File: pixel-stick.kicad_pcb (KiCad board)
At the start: 2 copper layers, 44 x 20.5 mm, 20 parts, among them J1 WS281*, J2 ISP, Q1 BSS138, SW1 RESET, SW2 PROG, U1 LM3670MF, U2 RT9361A, U4 ESP-M2

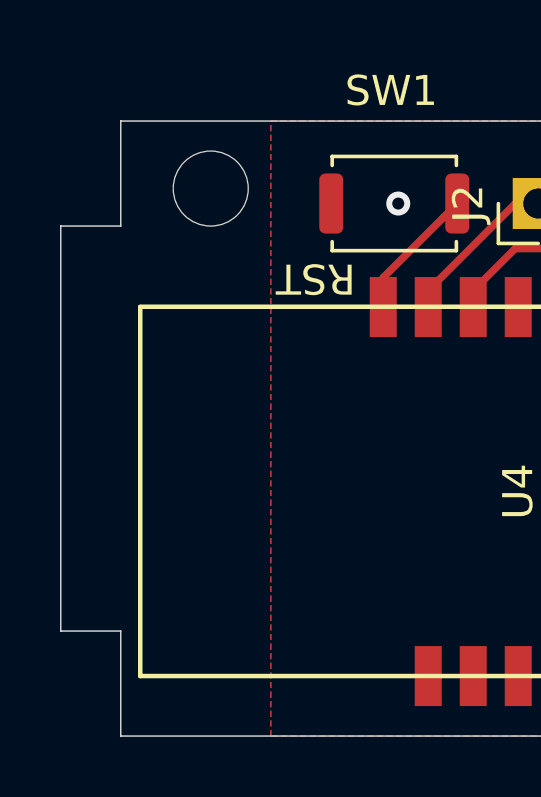
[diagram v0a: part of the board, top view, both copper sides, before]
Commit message: trim excess pcb
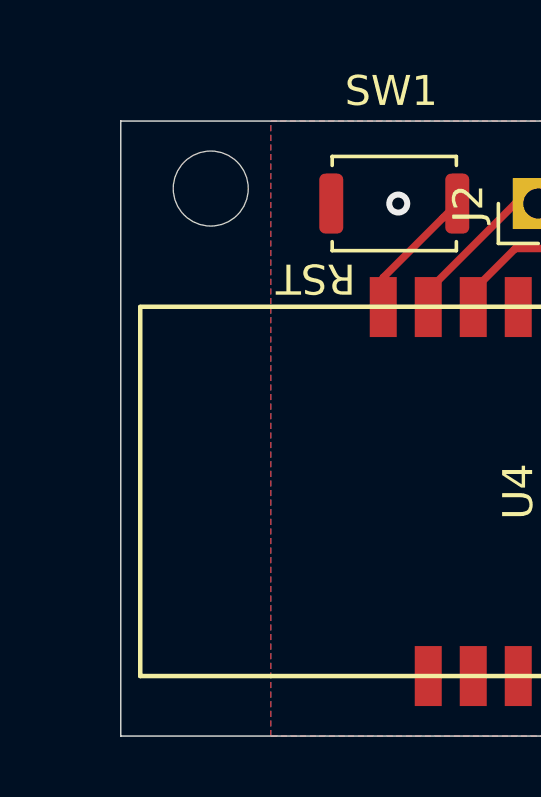
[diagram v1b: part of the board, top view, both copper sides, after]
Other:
- board size 44 x 20.5 mm -> 42 x 20.5 mm
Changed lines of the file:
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@@
   (general
     (thickness 1.6)
-    (drawings 18)
+    (drawings 14)
     (tracks 103)
     (zones 0)
@@
     )
   )
+  (gr_line (start 72 28.5) (end 72 49) (layer Edge.Cuts) (width 0.05))
   (gr_text RST (at 78.5 33.75 180) (layer F.SilkS)
     (effects (font (size 1 1) (thickness 0.15)))
@@
   (gr_line (start 110.5 30.2) (end 114 30.2) (layer Edge.Cuts) (width 0.05))
   (gr_line (start 110.5 28.5) (end 110.5 30.2) (layer Edge.Cuts) (width 0.05))
-  (gr_line (start 72 45.5) (end 70 45.5) (layer Edge.Cuts) (width 0.05))
-  (gr_line (start 72 49) (end 72 45.5) (layer Edge.Cuts) (width 0.05))
-  (gr_line (start 72 32) (end 70 32) (layer Edge.Cuts) (width 0.05))
-  (gr_line (start 72 28.5) (end 72 32) (layer Edge.Cuts) (width 0.05))
-  (gr_line (start 70 32) (end 70 45.5) (layer Edge.Cuts) (width 0.05))
   (gr_line (start 110.5 28.5) (end 72 28.5) (layer Edge.Cuts) (width 0.05))
   (gr_line (start 114 47.3) (end 114 30.2) (layer Edge.Cuts) (width 0.05))

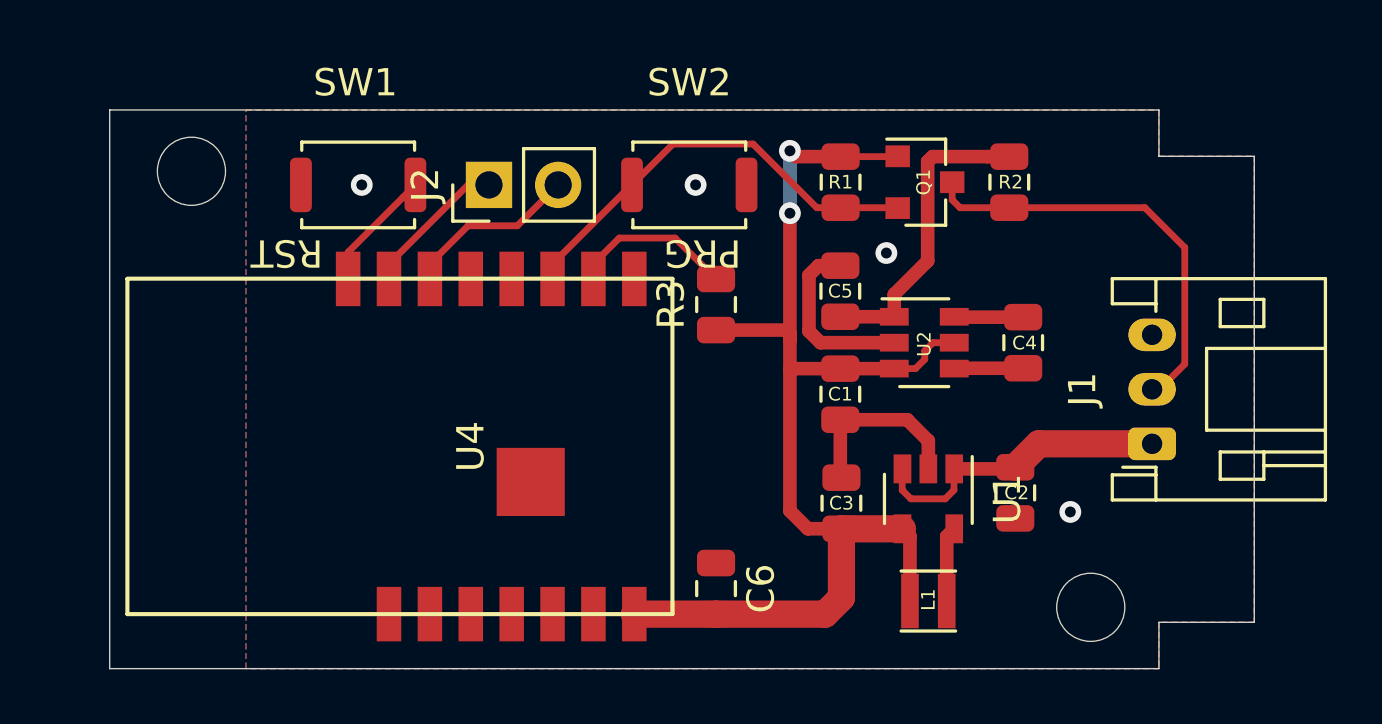
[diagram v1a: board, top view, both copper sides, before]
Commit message: make design work for ESP-01 or ESP-M2
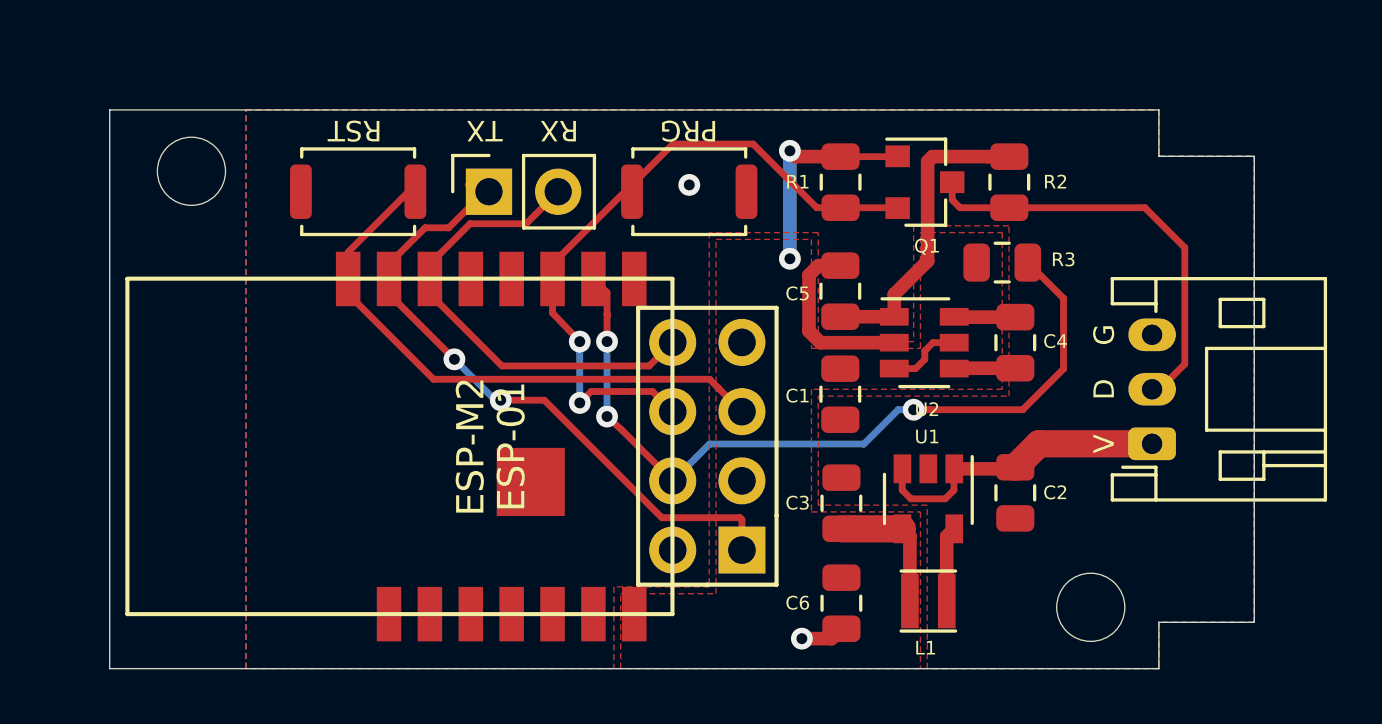
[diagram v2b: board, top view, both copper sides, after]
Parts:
- added ESP-01: ESP-01v090, ESP8266:ESP-01, F.Cu at (95.2, 44.6)
- J2: footprint Connector_PinHeader_2.54mm:PinHeader_1x02_P2.54mm_Vertical -> Connector_PinSocket_2.54mm:PinSocket_1x02_P2.54mm_Vertical
- moved R3 10.6 mm to (104.8, 34.1), turned to 0 degrees
- moved C6 4.63 mm to (98.8, 46.6), turned to 90 degrees
- moved C4 0.29 mm to (105.2, 37.0)
- moved J2 0.25 mm to (85.9, 31.5)
- moved SW1 0.25 mm to (81.1, 31.5)
- moved SW2 0.25 mm to (93.3, 31.5)
- renumbered U4 to ESP-M2
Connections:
- net Net-(R3-Pad2) renamed /GPIO2
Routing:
- net +3V3: track 44.4 -> 15.9 mm
- net /GPIO2: track 6.07 -> 30.5 mm, vias 0 -> 3
- net /TXD: track 5.42 -> 24.2 mm, vias 0 -> 2
- net /RST: track 4.47 -> 21.3 mm
- net /RXD: track 6.46 -> 17.3 mm
- net /GPIO0: track 16.0 -> 24.9 mm, vias 0 -> 2
- net GND: track 13.4 -> 8.26 mm, vias 4 -> 2
- added copper zone on F.Cu, net +3V3
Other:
- board text added: "D"
- board text added: "G"
- board text added: "RX"
- board text added: "TX"
- board text added: "V"

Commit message: remove resistor from GPIO2 pull-up
may have been a bad idea ... will need to check that things still work. Its possible the ESP-01 and ESP-M2 have internal pull ups alredy enabled and I can remove the external 3V3 entirely.
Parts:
- removed R3: 10k, Resistor_SMD:R_0805_2012Metric
- J2: footprint Connector_PinSocket_2.54mm:PinSocket_1x02_P2.54mm_Vertical -> Connector_PinHeader_2.54mm:PinHeader_1x02_P2.54mm_Vertical
- renumbered ESP-01 to U3, ESP-M2 to U4
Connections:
- U3 pad 4: /GPIO2 -> +3V3
- U4 pad 9: /GPIO2 -> +3V3
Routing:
- net /GPIO2: track 30.5 -> 0.00 mm, vias 3 -> 0
- net +3V3: track 15.9 -> 25.9 mm, vias 2 -> 4
- net /DATA: track 15.8 -> 11.9 mm
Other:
- board text added: "Board Version: 20191218a"
- board text removed: "Board Version: 20191217a"

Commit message: Add R3 back to GPIO2
Also re-laid out the microcontrollers in schematic to make it clearer how the common interface is achieved.
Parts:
- added R3: 10k, Resistor_SMD:R_0805_2012Metric, F.Cu at (104.3, 34.0)
- J2: value ISP -> ICSP
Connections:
- U3 pad 4: +3V3 -> /GPIO2
- U4 pad 9: +3V3 -> /GPIO2
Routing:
- net /GPIO2: track 0.00 -> 30.8 mm, vias 0 -> 3
- net +3V3: track 25.9 -> 15.9 mm, vias 4 -> 2
- net /DATA: track 11.9 -> 14.2 mm
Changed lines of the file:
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@@
     (thickness 1.6)
     (drawings 19)
-    (tracks 123)
+    (tracks 138)
     (zones 0)
-    (modules 20)
-    (nets 22)
+    (modules 21)
+    (nets 23)
   )
   (page A4)
@@
   (net 20 "Net-(U4-Pad2)")
   (net 21 "Net-(U3-Pad3)")
+  (net 22 /GPIO2)
   (net_class Default "This is the default net class."
     (clearance 0.2)
@@
     (add_net /DATA)
     (add_net /GPIO0)
+    (add_net /GPIO2)
     (add_net /RST)
     (add_net /RXD)
@@
     (add_net VIN)
   )
+  (module Resistor_SMD:R_0805_2012Metric (layer F.Cu)
+    (at 104.3125 34)
+    (descr "Resistor SMD 0805 (2012 Metric), square (rectangular) end terminal, IPC_7351 nominal, (Body size source: https://docs.google.com/spreadsheets/d/1BsfQQcO9C6DZCsRaXUlFlo91Tg2WpOkGARC1WS5S8t0/edit?usp=sharing), generated with kicad-footprint-generator")
+    (tags resistor)
+    (attr smd)
+    (fp_text reference R3 (at 2.3975 0) (layer F.SilkS)
+      (effects (font (size 0.5 0.5) (thickness 0.125)))
+    )
+    (fp_text value 10k (at 0 1.65) (layer F.Fab)
+      (effects (font (size 1 1) (thickness 0.15)))
+    )
+    (fp_text user %R (at 0 0) (layer F.Fab)
+      (effects (font (size 0.5 0.5) (thickness 0.08)))
+    )
+    (fp_line (start 1.68 0.95) (end -1.68 0.95) (layer F.CrtYd) (width 0.05))
+    (fp_line (start 1.68 -0.95) (end 1.68 0.95) (layer F.CrtYd) (width 0.05))
+    (fp_line (start -1.68 -0.95) (end 1.68 -0.95) (layer F.CrtYd) (width 0.05))
+    (fp_line (start -1.68 0.95) (end -1.68 -0.95) (layer F.CrtYd) (width 0.05))
+    (fp_line (start -0.258578 0.71) (end 0.258578 0.71) (layer F.SilkS) (width 0.12))
+    (fp_line (start -0.258578 -0.71) (end 0.258578 -0.71) (layer F.SilkS) (width 0.12))
+    (fp_line (start 1 0.6) (end -1 0.6) (layer F.Fab) (width 0.1))
+    (fp_line (start 1 -0.6) (end 1 0.6) (layer F.Fab) (width 0.1))
+    (fp_line (start -1 -0.6) (end 1 -0.6) (layer F.Fab) (width 0.1))
+    (fp_line (start -1 0.6) (end -1 -0.6) (layer F.Fab) (width 0.1))
+    (pad 2 smd roundrect (at 0.9375 0) (size 0.975 1.4) (layers F.Cu F.Paste F.Mask) (roundrect_rratio 0.25)
+      (net 22 /GPIO2))
+    (pad 1 smd roundrect (at -0.9375 0) (size 0.975 1.4) (layers F.Cu F.Paste F.Mask) (roundrect_rratio 0.25)
+      (net 2 +3V3))
+    (model ${KISYS3DMOD}/Resistor_SMD.3dshapes/R_0805_2012Metric.wrl
+      (at (xyz 0 0 0))
+      (scale (xyz 1 1 1))
+      (rotate (xyz 0 0 0))
+    )
+  )
   (module Connector_PinHeader_2.54mm:PinHeader_1x02_P2.54mm_Vertical locked (layer F.Cu)
     (at 85.917499 31.5 90)
@@
       (effects (font (size 1 1) (thickness 0.15)))
     )
-    (fp_text value ISP (at 0 4.87 90) (layer F.Fab)
+    (fp_text value ICSP (at 0 4.87 90) (layer F.Fab)
       (effects (font (size 1 1) (thickness 0.15)))
     )
@@
       (net 13 /RST))
     (pad 4 thru_hole oval (at 2.54 2.54 180) (size 1.7272 1.7272) (drill 1.016) (layers *.Cu *.Mask F.SilkS)
-      (net 2 +3V3))
+      (net 22 /GPIO2))
     (pad 3 thru_hole oval (at 0 2.54 180) (size 1.7272 1.7272) (drill 1.016) (layers *.Cu *.Mask F.SilkS)
       (net 21 "Net-(U3-Pad3)"))
@@
       (net 5 /GPIO0))
     (pad 9 smd rect (at 6.15 4.5 180) (size 0.9 2) (layers F.Cu F.Paste F.Mask)
-      (net 2 +3V3))
+      (net 22 /GPIO2))
     (pad 8 smd rect (at 6.15 6 180) (size 0.9 2) (layers F.Cu F.Paste F.Mask)
       (net 1 GND))
@@
   (segment (start 96.95998 30) (end 96.95998 33.95998) (width 0.5) (layer B.Cu) (net 2))
   (segment (start 96.95998 34.09002) (end 96.95998 33.95998) (width 0.5) (layer F.Cu) (net 2))
-  (segment (start 90.25 37) (end 90.25 36.9) (width 0.25) (layer B.Cu) (net 2))
-  (segment (start 90.25 36.9) (end 90.25 39.75) (width 0.25) (layer B.Cu) (net 2))
-  (segment (start 90.25 36) (end 90.25 35.2) (width 0.25) (layer F.Cu) (net 2))
-  (segment (start 90.275001 36.025001) (end 90.25 36) (width 0.25) (layer F.Cu) (net 2))
-  (segment (start 90.25 37) (end 90.25 36) (width 0.25) (layer F.Cu) (net 2))
-  (segment (start 90.25 35.2) (end 89.75 34.7) (width 0.25) (layer F.Cu) (net 2))
-  (via (at 90.25 39.75) (size 0.8) (drill 0.4) (layers F.Cu B.Cu) (net 2))
-  (segment (start 89.75 34.7) (end 89.75 35.25) (width 0.25) (layer F.Cu) (net 2))
-  (via (at 90.25 37) (size 0.8) (drill 0.4) (layers F.Cu B.Cu) (net 2))
-  (segment (start 90.8 40.25) (end 92.66 42.11) (width 0.25) (layer F.Cu) (net 2))
-  (segment (start 90.25 39.75) (end 90.8 40.25) (width 0.25) (layer F.Cu) (net 2))
-  (segment (start 89.75 34.7) (end 89.75 34.15) (width 0.25) (layer F.Cu) (net 2))
+  (segment (start 90.25 37) (end 90.25 36.9) (width 0.25) (layer B.Cu) (net 22))
+  (segment (start 90.25 36.9) (end 90.25 39.75) (width 0.25) (layer B.Cu) (net 22))
+  (segment (start 90.25 36) (end 90.25 35.2) (width 0.25) (layer F.Cu) (net 22))
+  (segment (start 90.275001 36.025001) (end 90.25 36) (width 0.25) (layer F.Cu) (net 22))
+  (segment (start 90.25 37) (end 90.25 36) (width 0.25) (layer F.Cu) (net 22))
+  (segment (start 90.25 35.2) (end 89.75 34.7) (width 0.25) (layer F.Cu) (net 22))
+  (via (at 90.25 39.75) (size 0.8) (drill 0.4) (layers F.Cu B.Cu) (net 22))
+  (segment (start 89.75 34.7) (end 89.75 35.25) (width 0.25) (layer F.Cu) (net 22))
+  (via (at 90.25 37) (size 0.8) (drill 0.4) (layers F.Cu B.Cu) (net 22))
+  (segment (start 90.8 40.25) (end 92.66 42.11) (width 0.25) (layer F.Cu) (net 22))
+  (segment (start 90.25 39.75) (end 90.8 40.25) (width 0.25) (layer F.Cu) (net 22))
+  (segment (start 89.75 34.7) (end 89.75 34.15) (width 0.25) (layer F.Cu) (net 22))
   (segment (start 100.785 36.085) (end 100.79 36.09) (width 0.5) (layer F.Cu) (net 3))
   (segment (start 100.7875 36.0875) (end 100.79 36.09) (width 0.5) (layer F.Cu) (net 3))
@@
   (segment (start 105.01 32.0875) (end 103.2025 32.0875) (width 0.25) (layer F.Cu) (net 4))
   (segment (start 109.975 38.75) (end 110.25 38.75) (width 0.25) (layer F.Cu) (net 4))
-  (segment (start 105.01 33.785) (end 109.975 38.75) (width 0.25) (layer F.Cu) (net 4))
-  (segment (start 105.01 32.0875) (end 105.01 33.785) (width 0.25) (layer F.Cu) (net 4))
+  (segment (start 107.131247 33.408747) (end 107.131247 38.618753) (width 0.25) (layer F.Cu) (net 4))
+  (segment (start 105.01 32.0875) (end 105.81 32.0875) (width 0.25) (layer F.Cu) (net 4))
+  (segment (start 105.81 32.0875) (end 107.131247 33.408747) (width 0.25) (layer F.Cu) (net 4))
+  (segment (start 107.262494 38.75) (end 110.25 38.75) (width 0.25) (layer F.Cu) (net 4))
+  (segment (start 107.131247 38.618753) (end 107.262494 38.75) (width 0.25) (layer F.Cu) (net 4))
   (segment (start 88.25 34.15) (end 91.15 31.25) (width 0.25) (layer F.Cu) (net 5))
   (segment (start 91.15 31.25) (end 91.167499 31.25) (width 0.25) (layer F.Cu) (net 5))
@@
   (segment (start 80.75 35.25) (end 83.881399 38.381399) (width 0.25) (layer F.Cu) (net 13))
   (segment (start 80.75 34.7) (end 80.75 35.25) (width 0.25) (layer F.Cu) (net 13))
+  (segment (start 106.681237 34.556237) (end 106.681237 38.030613) (width 0.25) (layer F.Cu) (net 22))
+  (segment (start 106.125 34) (end 106.681237 34.556237) (width 0.25) (layer F.Cu) (net 22))
+  (segment (start 105.480925 39.230925) (end 100.519075 39.230925) (width 0.25) (layer F.Cu) (net 22))
+  (segment (start 106.681237 38.030613) (end 105.480925 39.230925) (width 0.25) (layer F.Cu) (net 22))
+  (segment (start 100.519075 39.230925) (end 100.519075 39.230925) (width 0.25) (layer F.Cu) (net 22))
+  (via (at 100.519075 39.230925) (size 0.8) (drill 0.4) (layers F.Cu B.Cu) (net 22))
+  (segment (start 106.125 34) (end 105.25 34) (width 0.25) (layer F.Cu) (net 22))
+  (segment (start 93.523599 41.246401) (end 92.66 42.11) (width 0.25) (layer B.Cu) (net 22))
+  (segment (start 93.848601 40.921399) (end 93.523599 41.246401) (width 0.25) (layer B.Cu) (net 22))
+  (segment (start 95.607731 40.921399) (end 93.848601 40.921399) (width 0.25) (layer B.Cu) (net 22))
+  (segment (start 97.298205 39.230925) (end 95.607731 40.921399) (width 0.25) (layer B.Cu) (net 22))
+  (segment (start 100.519075 39.230925) (end 97.298205 39.230925) (width 0.25) (layer B.Cu) (net 22))
   (zone (net 1) (net_name GND) (layer B.Cu) (hatch edge 0.508)
     (connect_pads (clearance 0.5))

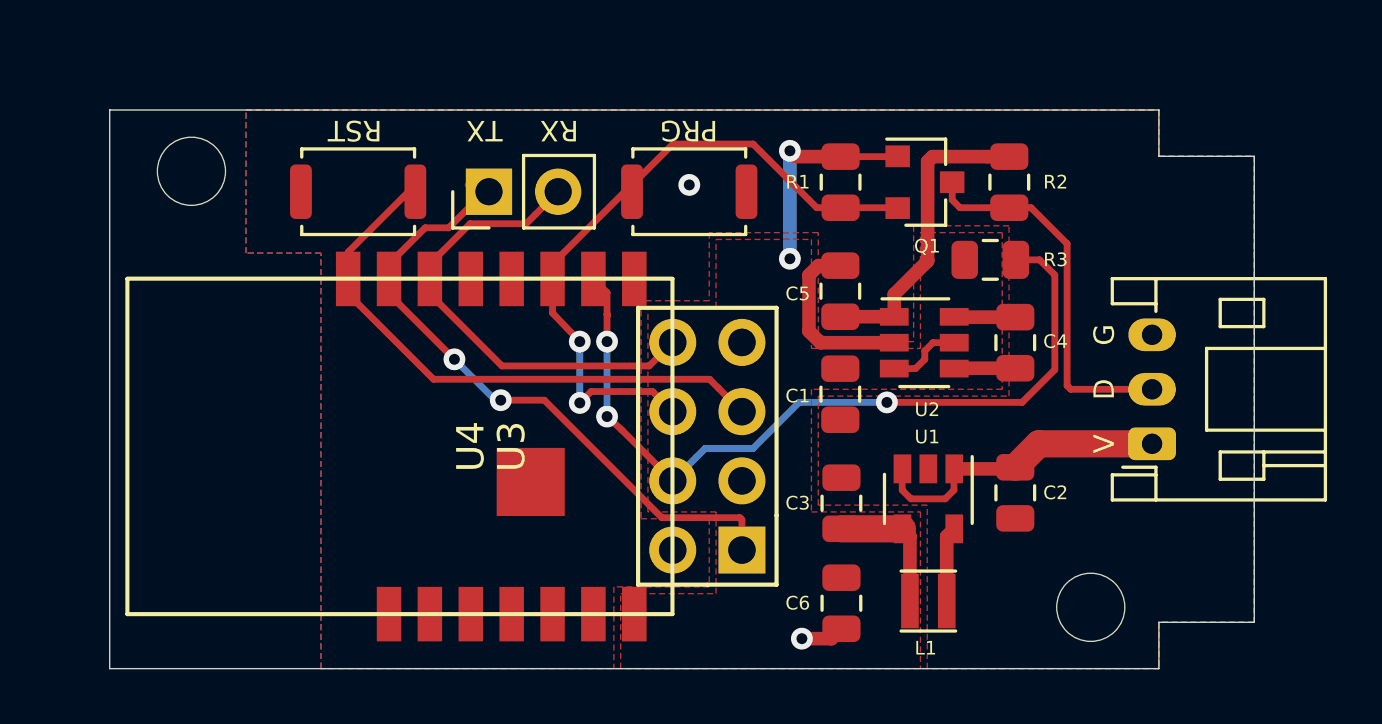
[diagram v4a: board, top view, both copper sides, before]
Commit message: simplify programming
pull the buttons and all pins necessary off the board. A programming adapter will need to be made.
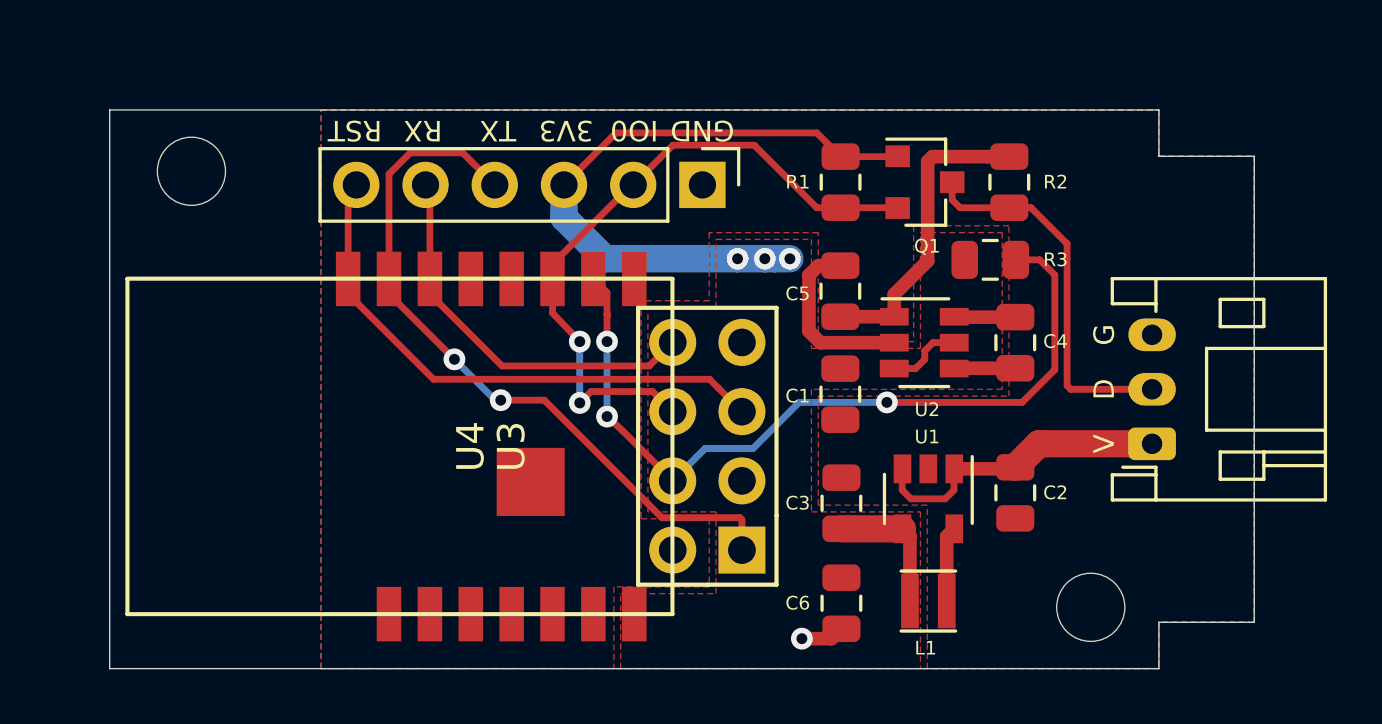
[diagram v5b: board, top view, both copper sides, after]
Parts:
- removed SW1: RESET, Button_Switch_SMD:SW_Push_SPST_NO_Alps_SKRK
- removed SW2: PROG, Button_Switch_SMD:SW_Push_SPST_NO_Alps_SKRK
- J2: value ICSP -> UART; footprint Connector_PinHeader_2.54mm:PinHeader_1x02_P2.54mm_Vertical -> Connector_PinHeader_2.54mm:PinHeader_1x06_P2.54mm_Vertical
- moved J2 7.84 mm to (93.8, 31.2), turned to 270 degrees
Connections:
- J2 pad 1: /TXD -> GND
- J2 pad 2: /RXD -> /GPIO0
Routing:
- net +3V3: track 15.9 -> 31.4 mm, vias 2 -> 3
- net /TXD: track 24.2 -> 27.2 mm
- net /RXD: track 17.3 -> 15.0 mm
- net /RST: track 21.3 -> 19.8 mm
- net GND: vias 2 -> 1
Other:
- board text added: "3V3"
- board text added: "GND"
- board text added: "IO0"
- board text removed: "PRG"
